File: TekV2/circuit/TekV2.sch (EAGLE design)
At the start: 7 parts, among them IC1 74HC74N, IC2 74LS32N

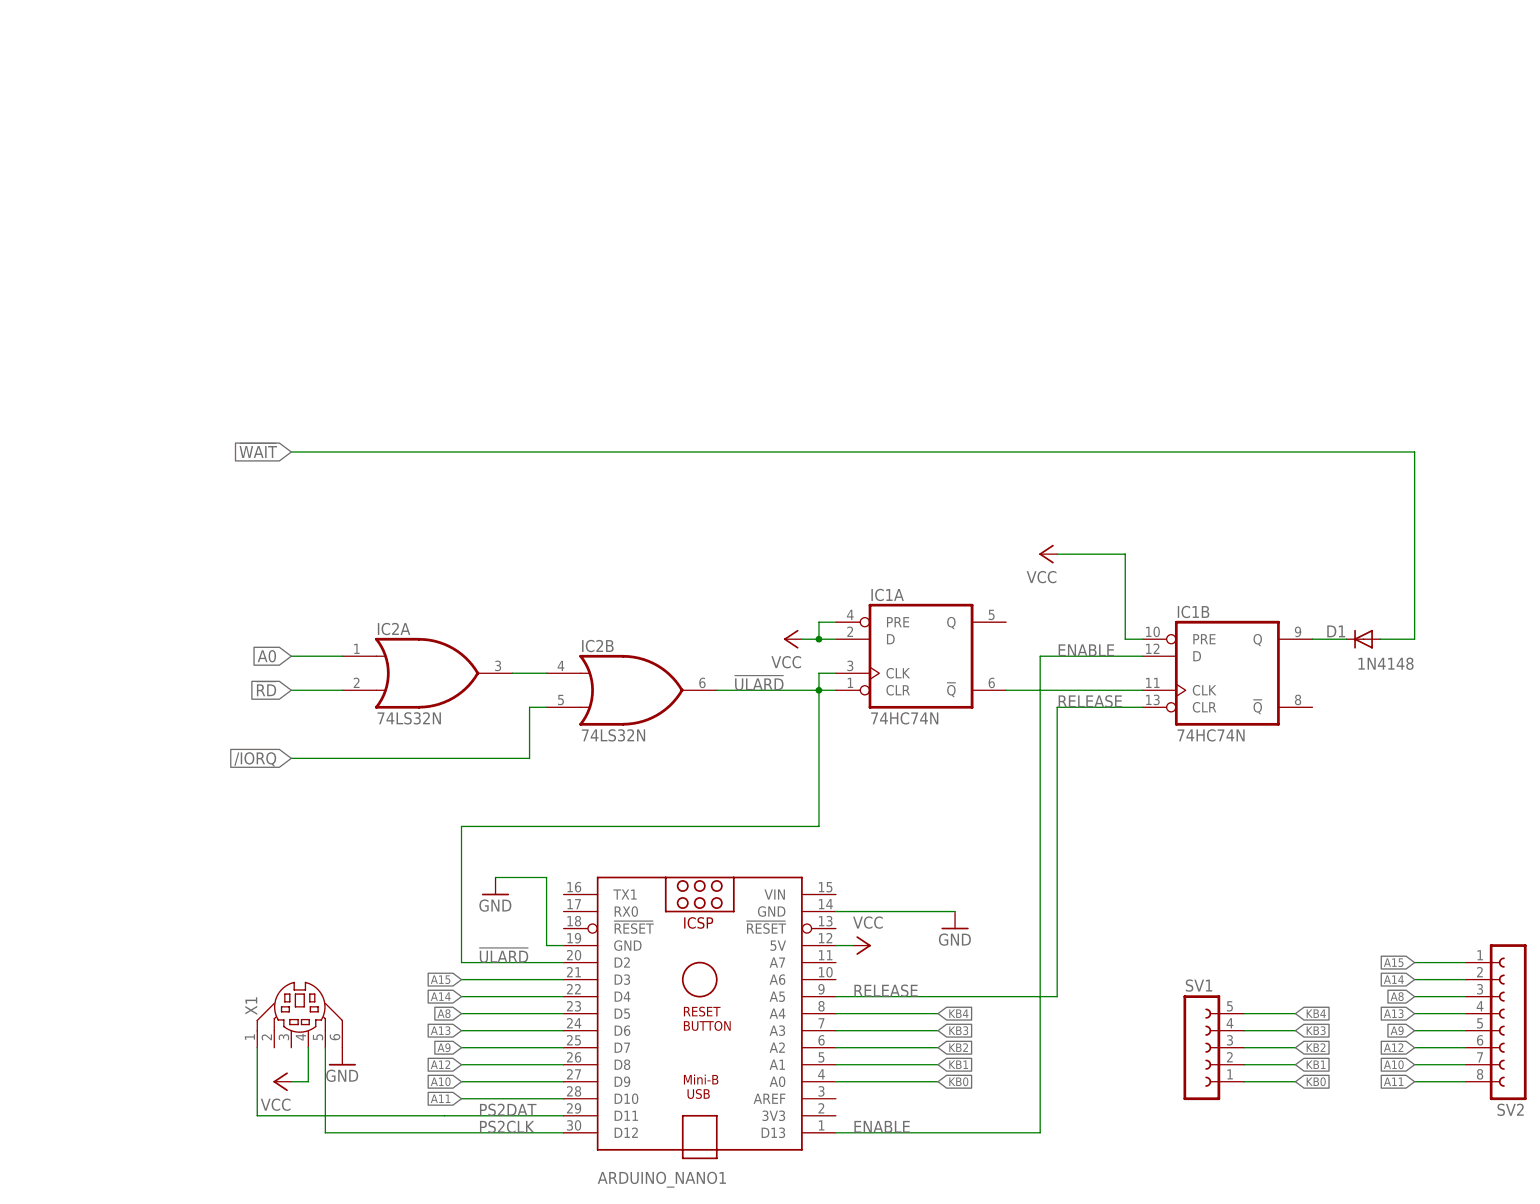
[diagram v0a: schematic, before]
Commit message: fixed connection of diode
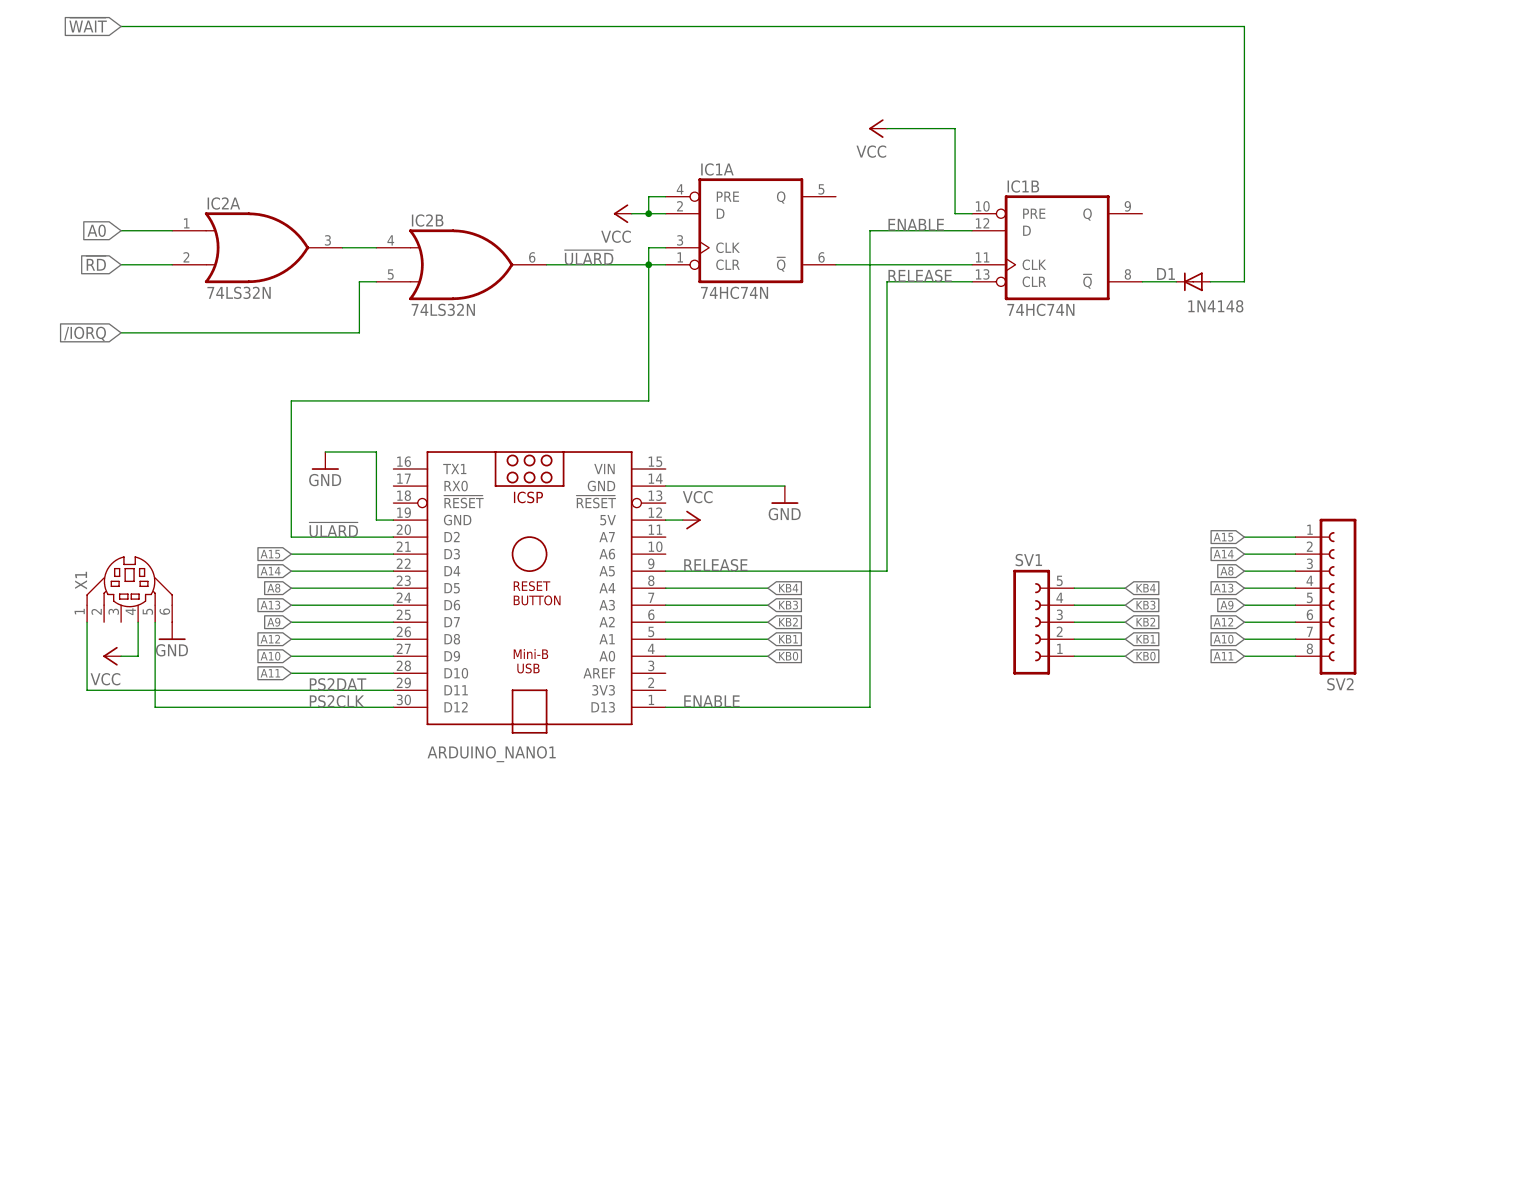
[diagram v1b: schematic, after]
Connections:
- net N$2: now also IC1B.!Q; no longer IC1B.Q
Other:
- moved on the sheet: ARDUINO_NANO1, D1, IC1A, IC1B, IC2A, IC2B, SV1, SV2, X1
